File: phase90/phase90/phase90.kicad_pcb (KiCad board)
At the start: 4 copper layers, 54.4 x 32 mm, 64 parts, among them J1 Conn_02x08_Odd_Even, Q1 Q_NJFET_DSG, Q2 Q_NJFET_DSG, Q3 Q_NJFET_DSG, Q4 Q_NJFET_DSG, U1 TL071HIDBVR, U10 TL071HIDBVR, U11 TL071HIDBVR, U12 AD5290, U2 TL071HIDBVR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

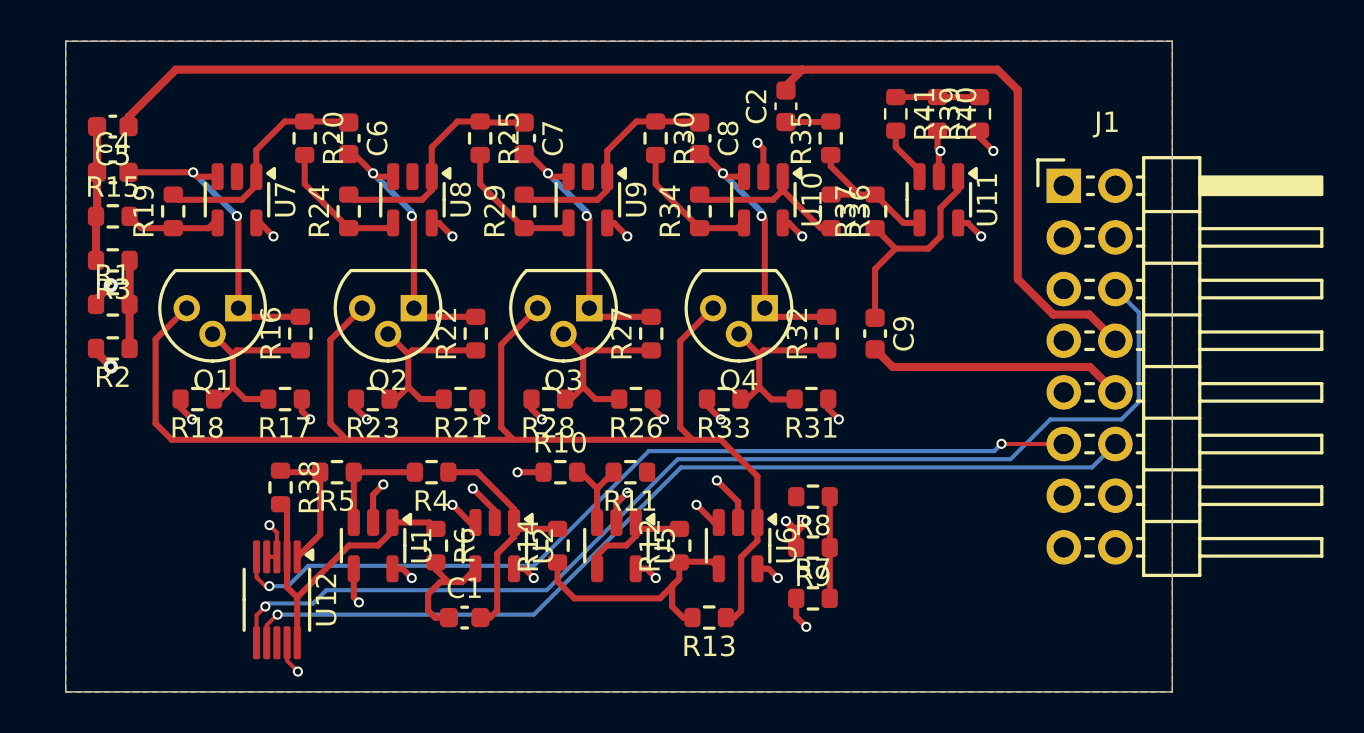
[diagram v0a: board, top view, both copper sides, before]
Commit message: silks have been scooted
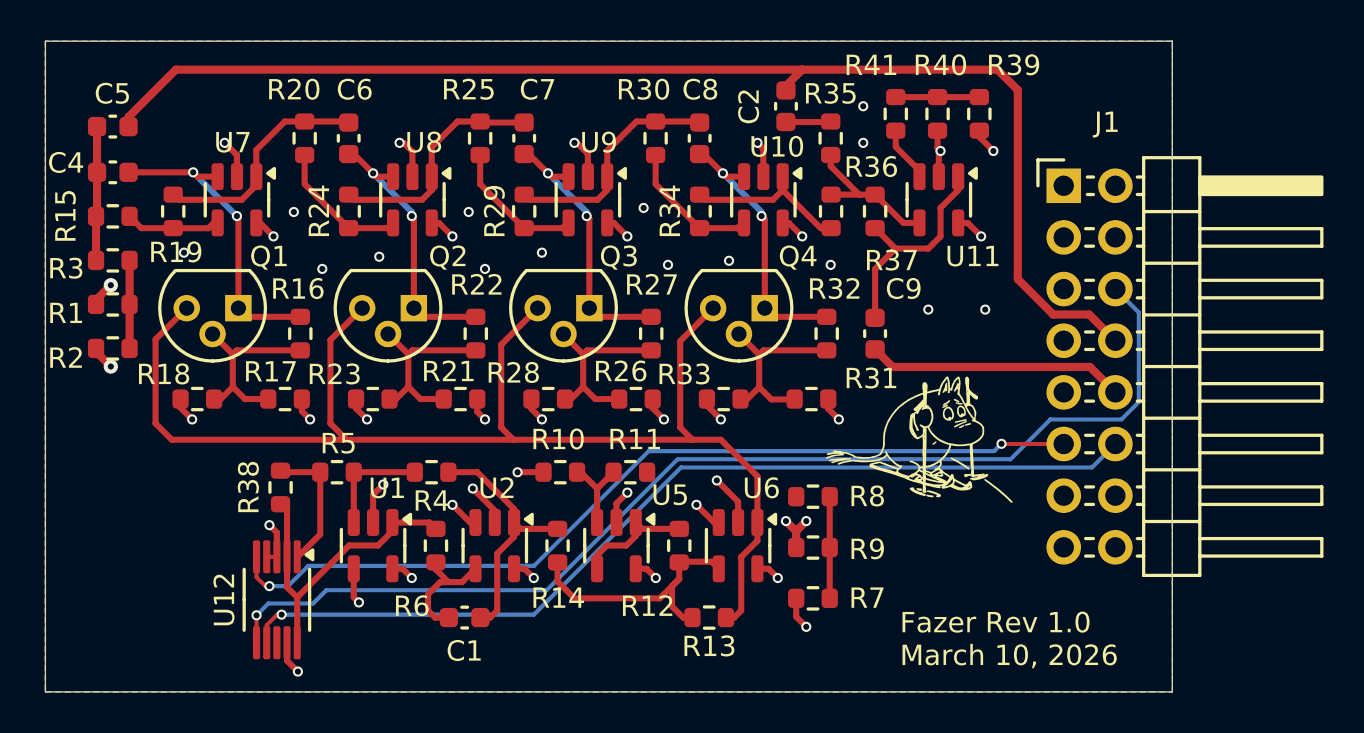
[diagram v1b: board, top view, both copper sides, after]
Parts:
- added G***: LOGO, LOGO, F.Cu at (122.2, 99.4)
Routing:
- net GND: track 20.9 -> 26.9 mm, vias 12 -> 30
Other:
- board size 54.4 x 32 mm -> 55.4 x 32 mm
- board text added: "Fazer Rev 1.0 March 10, 2026"
- board text added: "{dblquote}Can I get the purple one? Wait no, can I get the purple one?{dblquote} -Kyle de Nobel {dblquote}Frankly...{dblquote} - Marco Yaipen"
